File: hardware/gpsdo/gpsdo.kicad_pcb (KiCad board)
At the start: 4 copper layers, 70 x 70 mm, 88 parts, among them J1 Conn_01x02, J2 Conn_02x03_Top_Bottom, J3 USB_C_Receptacle_USB2.0_14P, J4 Conn_01x03, J5 Conn_Coaxial, U1 74HC4040D_652, U2 74HC4040D_652, U3 REF5040AD, U4 AD5541A, U5 OPA197xD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

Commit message: final changes
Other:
- board text added: "DEBUG"

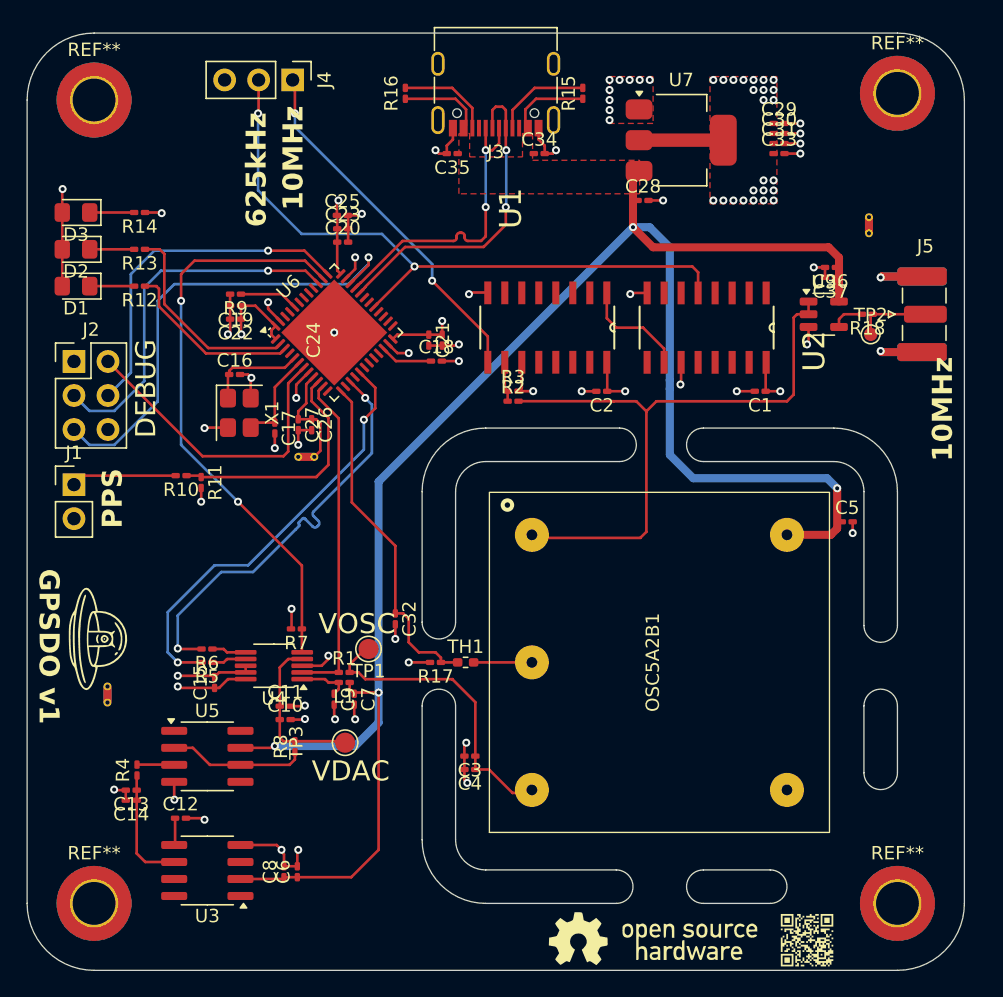
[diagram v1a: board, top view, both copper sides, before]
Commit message: cleanup; remove references from silkscreen
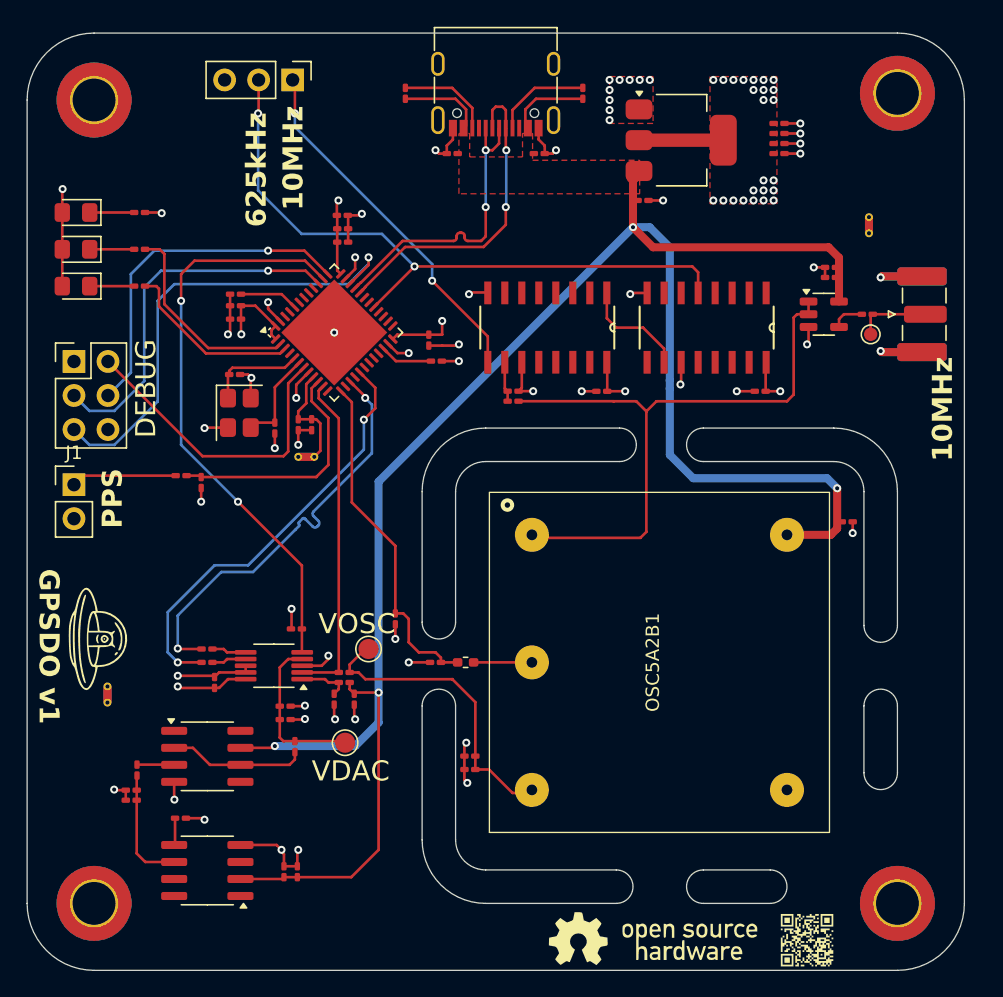
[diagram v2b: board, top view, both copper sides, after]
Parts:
- removed C24: 100n, Capacitor_SMD:C_0201_0603Metric_Pad0.64x0.40mm_HandSolder
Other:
- board text added: "${REFERENCE}"

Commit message: update pcb
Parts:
- added C24: 100n, Capacitor_SMD:C_0201_0603Metric_Pad0.64x0.40mm_HandSolder, F.Cu at (138.8, 87.7)
- moved C34 0.75 mm to (146.0, 74.5)
- moved C35 0.75 mm to (139.5, 74.5)
- moved J3 0.75 mm to (142.8, 68.9)
- moved R15 0.75 mm to (149.2, 70.0)
- moved R16 0.75 mm to (136.0, 70.0)
- moved C28 0.50 mm to (153.8, 77.8)
- moved C29 0.50 mm to (163.9, 72.0)
- moved C30 0.50 mm to (163.9, 72.8)
- moved C31 0.50 mm to (163.9, 73.5)
- moved C33 0.50 mm to (163.9, 74.2)
- moved U7 0.50 mm to (156.6, 73.2)
- moved C3 0.21 mm to (141.0, 118.7)
- moved C4 0.21 mm to (141.0, 119.7)
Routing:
- net GNDA: track 42.3 -> 41.2 mm
- net USB_P: track 22.6 -> 21.8 mm
- net USB_N: track 24.2 -> 23.5 mm
- net GND: track 54.7 -> 55.2 mm
